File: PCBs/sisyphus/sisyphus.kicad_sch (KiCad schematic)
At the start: 31 parts, among them J1 USB_BOOT, J2 SWD, U1 W25Q128JVS, U2 RP2040, Y1 ABM8-272-T3

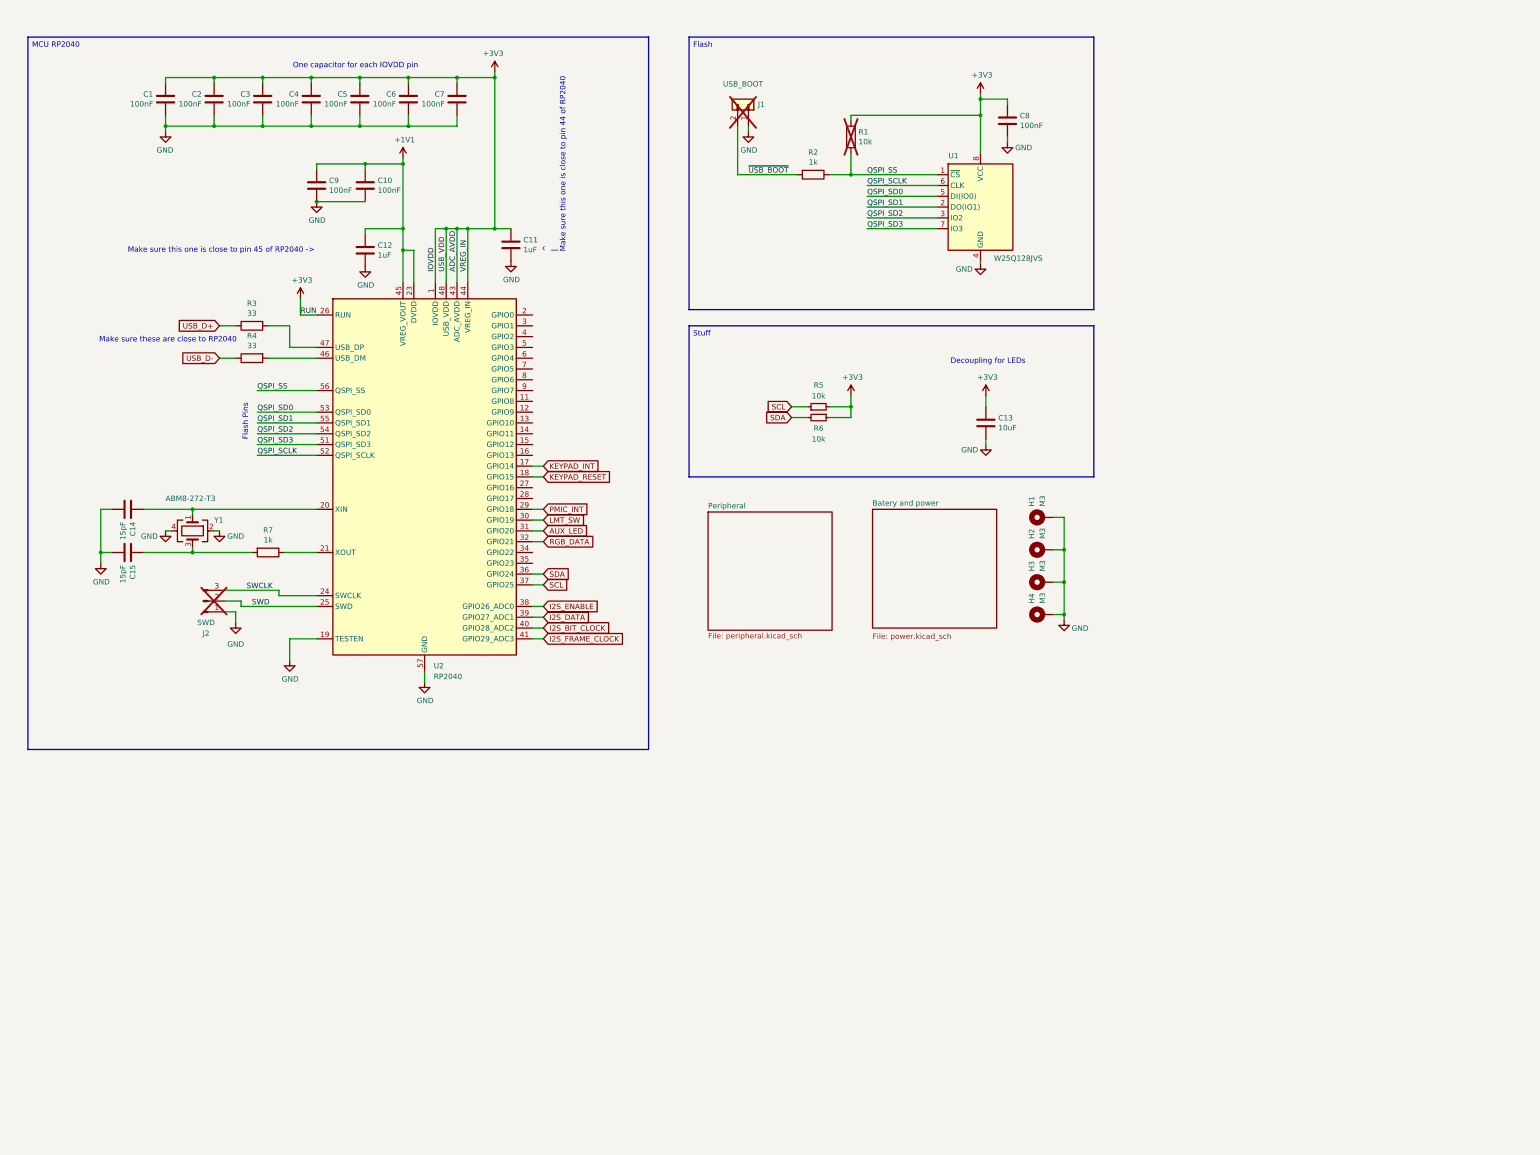
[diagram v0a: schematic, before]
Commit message: Add initial changes for Gamma
Merge all papers into one A3

Move I2S pins

Make more readable

Prepare connectors for new AUX board
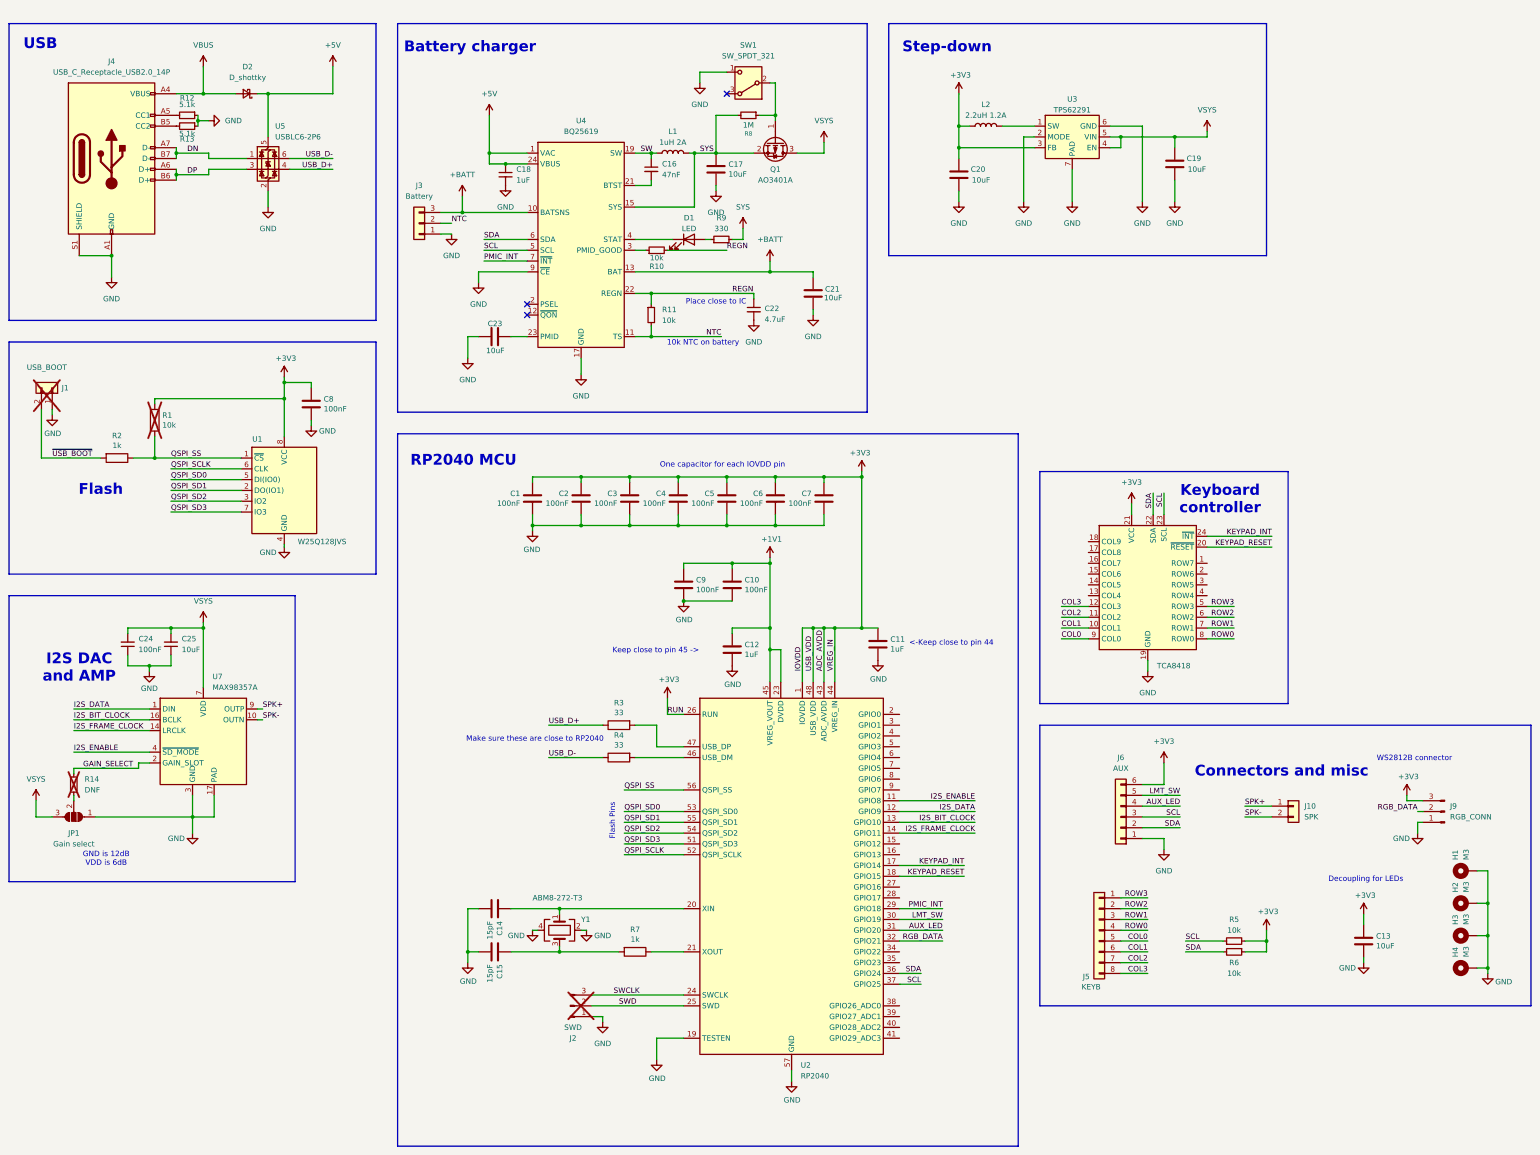
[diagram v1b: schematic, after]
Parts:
- added C16: 47nF, Capacitor_SMD:C_0402_1005Metric, symbol Device:C_Small
- added C17, C19, C20, C21, C23: 10uF, Capacitor_SMD:C_0402_1005Metric, symbol Device:C
- added C18: 1uF, Capacitor_SMD:C_0402_1005Metric, symbol Device:C_Small
- added C22: 4.7uF, Capacitor_SMD:C_0402_1005Metric, symbol Device:C_Small
- added C24: 100nF, Capacitor_SMD:C_0402_1005Metric, symbol Device:C_Small
- added C25: 10uF, Capacitor_SMD:C_0402_1005Metric, symbol Device:C_Small
- added D1: LED, LED_SMD:LED_0603_1608Metric, symbol Device:LED
- added D2: D_shottky, Diode_SMD:D_SOD-123, symbol Device:D_Schottky_Small
- added J10: SPK, Connector_PinHeader_2.54mm:PinHeader_1x02_P2.54mm_Vertical, symbol Connector_Generic:Conn_01x02
- added J3: Battery, Connector_JST:JST_PH_S3B-PH-SM4-TB_1x03-1MP_P2.00mm_Horizontal, symbol Connector_Generic:Conn_01x03
- added J4: USB_C_Receptacle_USB2.0_14P, Connector_USB:USB_C_Receptacle_G-Switch_GT-USB-7010ASV, symbol Connector:USB_C_Receptacle_USB2.0_14P
- added J5: KEYB, Connector_JST:JST_XH_S8B-XH-A_1x08_P2.50mm_Horizontal, symbol Connector_Generic:Conn_01x08
- added J6: AUX, symbol Connector_Generic:Conn_01x06
- added J9: RGB_CONN, Connector_PinHeader_2.54mm:PinHeader_1x03_P2.54mm_Vertical, symbol Connector:Conn_01x03_Pin
- added JP1: Gain select, Jumper:SolderJumper-3_P1.3mm_Open_RoundedPad1.0x1.5mm, symbol Jumper:SolderJumper_3_Open
- added L1: 1uH 2A, Inductor_SMD:L_0603_1608Metric, symbol Device:L
- added L2: 2.2uH 1.2A, Inductor_SMD:L_0805_2012Metric, symbol Device:L
- added Q1: AO3401A, Package_TO_SOT_SMD:SOT-23, symbol Transistor_FET:AO3401A
- added R10, R11: 10k, Resistor_SMD:R_0402_1005Metric, symbol Device:R_Small
- added R12, R13: 5.1k, Resistor_SMD:R_0402_1005Metric, symbol Device:R_Small
- added R14: DNF, Resistor_SMD:R_0402_1005Metric, symbol Device:R_Small
- added R8: 1M, Resistor_SMD:R_0402_1005Metric, symbol Device:R_Small
- added R9: 330, Resistor_SMD:R_0402_1005Metric, symbol Device:R_Small
- added SW1: SW_SPDT_321, Connector_PinHeader_2.54mm:PinHeader_1x03_P2.54mm_Vertical, symbol Switch:SW_SPDT_321
- added U3: TPS62291, Package_SON:WSON-6-1EP_2x2mm_P0.65mm_EP1x1.6mm_ThermalVias, symbol Sisyphus:TPS62293
- added U4: BQ25619, Package_DFN_QFN:Texas_RTW_WQFN-24-1EP_4x4mm_P0.5mm_EP2.7x2.7mm_ThermalVias, symbol Sisyphus:BQ25619
- added U5: USBLC6-2P6, Package_TO_SOT_SMD:SOT-666, symbol Power_Protection:USBLC6-2P6
- added U6: TCA8418, Package_DFN_QFN:WQFN-24-1EP_4x4mm_P0.5mm_EP2.45x2.45mm, symbol Sisyphus:TCA8418
- added U7: MAX98357A, Package_DFN_QFN:TQFN-16-1EP_3x3mm_P0.5mm_EP1.23x1.23mm, symbol Audio:MAX98357A
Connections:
- net +3V3: now also C20.1, J6.6 (Pin_6), J9.3 (Pin_3), L2.1, U3.3 (FB), U6.21 (VCC)
- net AUX_LED: now also J6.4 (Pin_4)
- net GND: now also C17.2, C18.2, C19.2, C20.2, C21.2, C22.2, C23.1, C24.1, C25.1, J3.1 (Pin_1), J4.A1 (GND), J4.A12 (GND), J4.B1 (GND), J4.B12 (GND), J4.S1 (SHIELD), J6.1 (Pin_1), J9.1 (Pin_1), JP1.1 (A), R12.1, R13.1, SW1.1 (C), U3.2 (MODE), U3.6 (GND), U3.7 (PAD), U4.17 (GND), U4.18 (GND), U4.25 (GND), U4.9 (~{CE}), U5.2 (GND), U6.19 (GND), U6.25 (PAD), U7.11 (GND), U7.15 (GND), U7.17 (PAD), U7.3 (GND)
- net I2S_BIT_CLOCK: now also U2.13 (GPIO10), U7.16 (BCLK); no longer U2.40 (GPIO28_ADC2)
- net I2S_DATA: now also U2.12 (GPIO9), U7.1 (DIN); no longer U2.39 (GPIO27_ADC1)
- net I2S_ENABLE: now also U2.11 (GPIO8), U7.4 (~{SD_MODE}); no longer U2.38 (GPIO26_ADC0)
- net I2S_FRAME_CLOCK: now also U2.14 (GPIO11), U7.14 (LRCLK); no longer U2.41 (GPIO29_ADC3)
- net KEYPAD_INT: now also U6.24 (~{INT})
- net KEYPAD_RESET: now also U6.20 (~{RESET})
- net LMT_SW: now also J6.5 (Pin_5)
- net PMIC_INT: now also U4.7 (~{INT})
- net RGB_DATA: now also J9.2 (Pin_2)
- net SCL: now also J6.3 (Pin_3), U4.5 (SCL), U6.23 (SCL)
- net SDA: now also J6.2 (Pin_2), U4.6 (SDA), U6.22 (SDA)
- net USB_D+: now also U5.4 (I/O2)
- net USB_D-: now also U5.6 (I/O1)
- new net: C16.2, U4.21 (BTST)
- new net: C23.2, U4.23 (PMID)
- new net: R10.1, U4.3 (PMID_GOOD)
- new net: D1.1 (K), U4.4 (STAT)
- new net: J4.B5 (CC2), R13.2
- new net: Q1.1 (G), R8.1, SW1.2 (B)
- new net: JP1.2 (C), R14.2
- new net: L2.2, U3.1 (SW)
- new net: J4.A5 (CC1), R12.2
- new net: D1.2 (A), R9.1
- new net +5V: C18.1, D2.1 (K), U4.1 (VAC), U4.24 (VBUS), U5.5 (VBUS)
- new net +BATT: C21.1, J3.3 (Pin_3), U4.10 (BATSNS), U4.13 (BAT), U4.14 (BAT)
- new net COL0: J5.5 (Pin_5), U6.9 (COL0)
- new net COL1: J5.6 (Pin_6), U6.10 (COL1)
- new net COL2: J5.7 (Pin_7), U6.11 (COL2)
- new net COL3: J5.8 (Pin_8), U6.12 (COL3)
- new net DN: J4.A7 (D-), J4.B7 (D-), U5.1 (I/O1)
- new net DP: J4.A6 (D+), J4.B6 (D+), U5.3 (I/O2)
- new net GAIN_SELECT: R14.1, U7.2 (GAIN_SLOT)
- new net NTC: J3.2 (Pin_2), R11.2, U4.11 (TS)
- new net REGN: C22.1, R10.2, R11.1, U4.22 (REGN)
- new net ROW0: J5.4 (Pin_4), U6.8 (ROW0)
- new net ROW1: J5.3 (Pin_3), U6.7 (ROW1)
- new net ROW2: J5.2 (Pin_2), U6.6 (ROW2)
- new net ROW3: J5.1 (Pin_1), U6.5 (ROW3)
- new net SPK+: J10.1 (Pin_1), U7.9 (OUTP)
- new net SPK-: J10.2 (Pin_2), U7.10 (OUTN)
- new net SW: C16.1, L1.1, U4.19 (SW), U4.20 (SW)
- new net SYS: C17.1, L1.2, Q1.2 (S), R8.2, R9.2, U4.15 (SYS), U4.16 (SYS)
- new net VBUS: D2.2 (A), J4.A4 (VBUS), J4.A9 (VBUS), J4.B4 (VBUS), J4.B9 (VBUS)
- new net VSYS: C19.1, C24.2, C25.2, JP1.3 (B), Q1.3 (D), U3.4 (EN), U3.5 (VIN), U7.7 (VDD), U7.8 (VDD)
- no-connect marks 0 -> 3
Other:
- removed sheet Batery and power
- removed sheet Peripheral
- note added: "10k NTC on battery"
- note added: "<-Keep close to pin 44"
- note added: "Battery charger"
- note added: "Connectors and misc"
- note added: "Flash"
- note added: "GND is 12dB VDD is 6dB"
- note added: "I2S DAC and AMP"
- note added: "Keep close to pin 45 ->"
- note added: "Keyboard controller"
- note added: "Place close to IC"
- note added: "RP2040 MCU"
- note added: "Step-down"
- note added: "USB"
- note added: "WS2812B connector"
- note removed: "Make sure this one is close to pin 45 of RP2040 ->"
- note removed: "^ | Make sure this one is close to pin 44 of RP2040"
- moved on the sheet: C1, C10, C11, C12, C13, C14, C15, C2, C3, C4, C5, C6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
